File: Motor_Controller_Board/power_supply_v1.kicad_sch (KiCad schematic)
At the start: 21 parts, among them J1 Conn_01x02, J2 Conn_01x02, SW1 SW_Push, U1 LM2596S-5, U2 ESP32-C3-WROOM-02U, U3 AMS1117

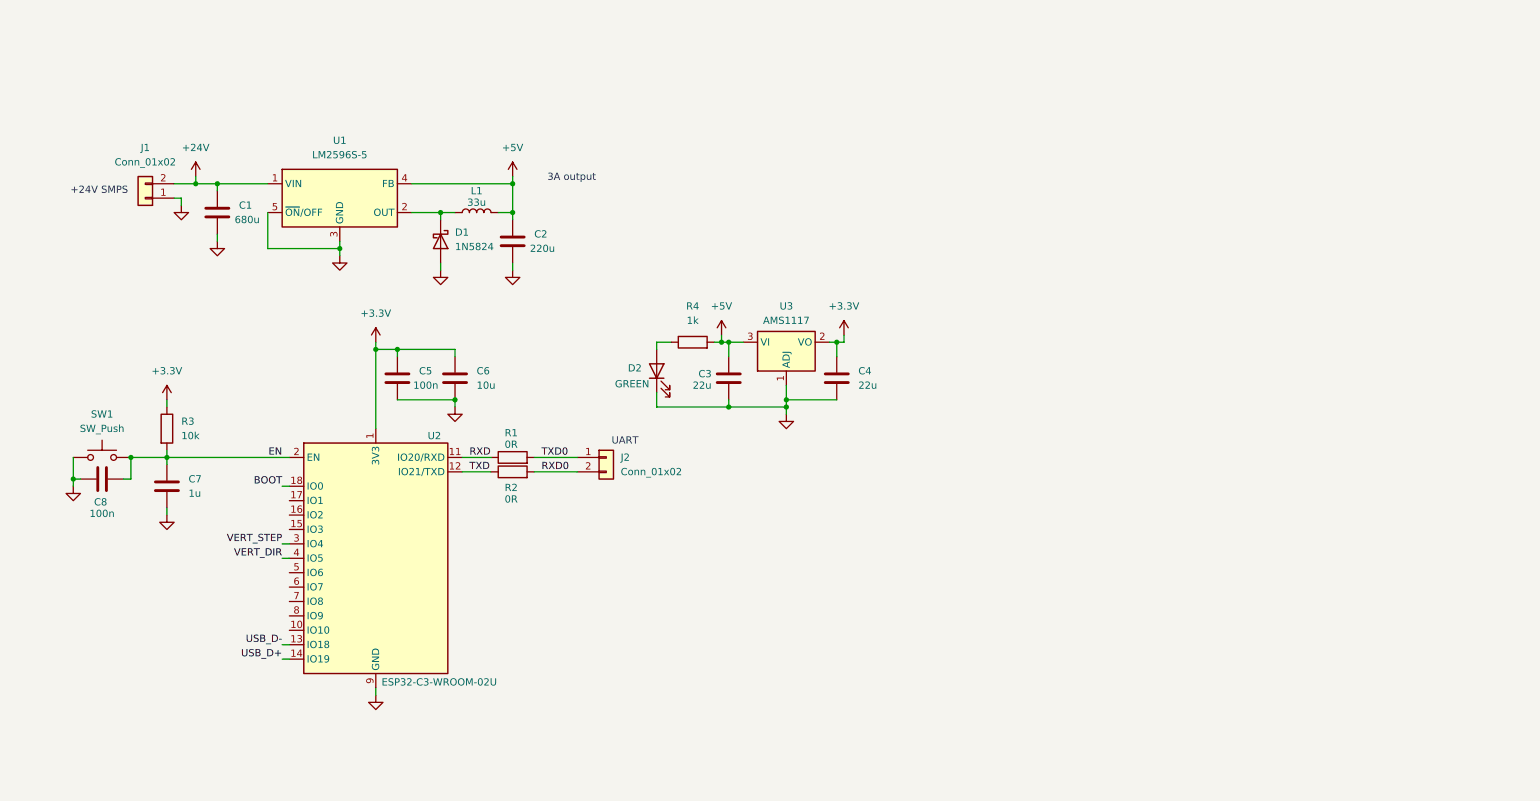
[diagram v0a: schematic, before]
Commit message: still dont know if these files can even be accessed, but the rough draft of schematic is finished. it needs revision to verify it will actually work. i made a top level page with three supporting pages for buck, microcontroller, and stepper drivers.
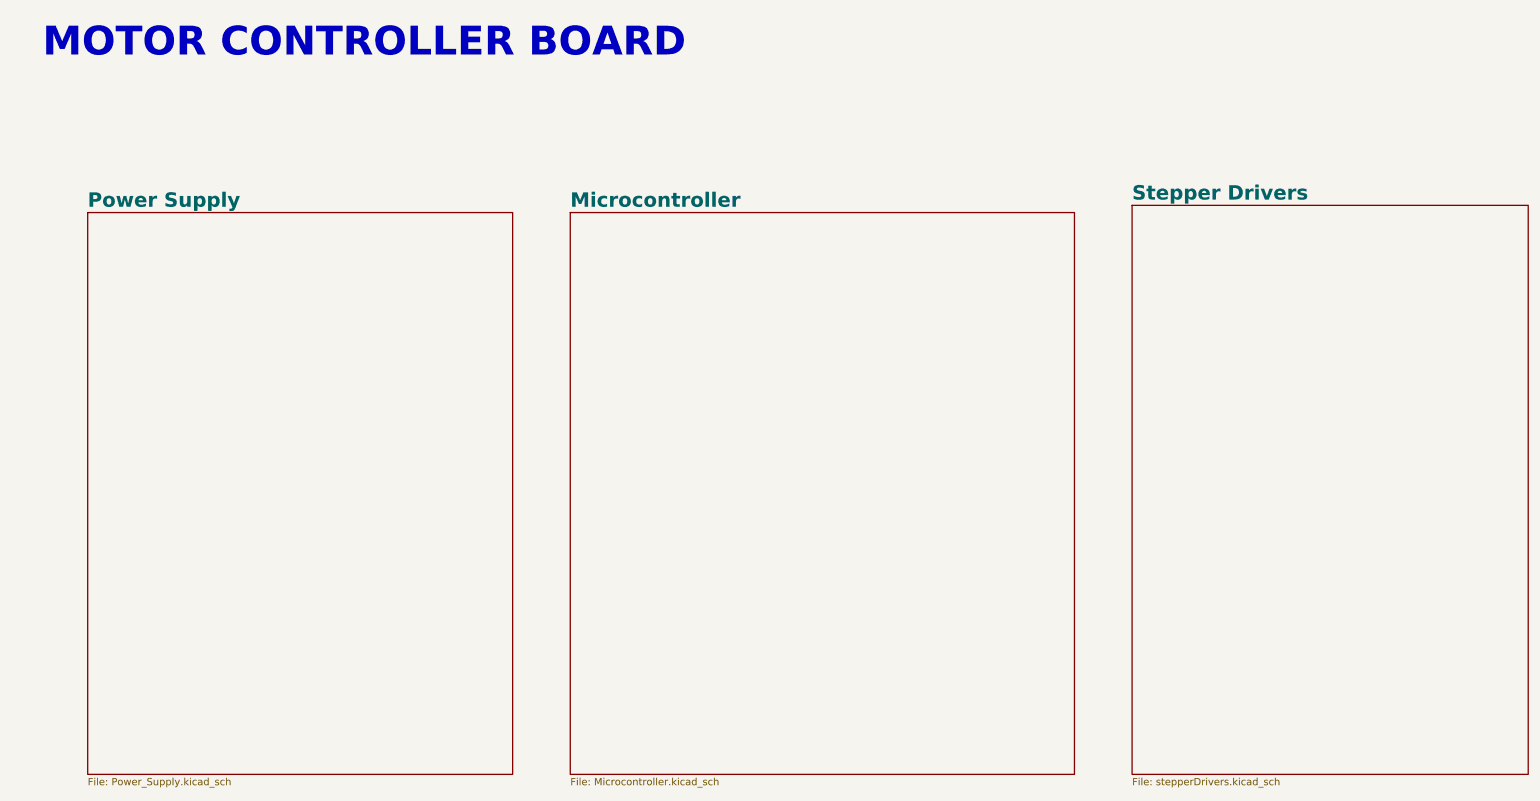
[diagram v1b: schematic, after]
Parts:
- removed C1: 680u, symbol Device:C
- removed C2: 220u, symbol Device:C
- removed C3, C4: 22u, symbol Device:C
- removed C5, C8: 100n, symbol Device:C
- removed C6: 10u, symbol Device:C
- removed C7: 1u, symbol Device:C
- removed D1: 1N5824, symbol Device:D_Schottky
- removed D2: GREEN, symbol Device:LED
- removed J1, J2: Conn_01x02, symbol Connector_Generic:Conn_01x02
- removed L1: 33u, symbol Device:L
- removed R1, R2: 0R, symbol Device:R
- removed R3: 10k, symbol Device:R
- removed R4: 1k, symbol Device:R
- removed SW1: SW_Push, symbol Switch:SW_Push
- removed U1: LM2596S-5, Package_TO_SOT_SMD:TO-263-5_TabPin3, symbol Regulator_Switching:LM2596S-5
- removed U2: ESP32-C3-WROOM-02U, RF_Module:ESP32-C3-WROOM-02U, symbol RF_Module:ESP32-C3-WROOM-02U
- removed U3: AMS1117, Package_TO_SOT_SMD:SOT-223-3_TabPin2, symbol Regulator_Linear:AMS1117
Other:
- added sheet Microcontroller (Microcontroller.kicad_sch)
- added sheet Power Supply (Power_Supply.kicad_sch)
- added sheet Stepper Drivers (stepperDrivers.kicad_sch)
- note added: "MOTOR CONTROLLER BOARD"
- note removed: "+24V SMPS"
- note removed: "3A output"
- note removed: "UART"
- company: (none) -> University of California, Santa Cruz
- title: (none) -> Motor Controller Board
